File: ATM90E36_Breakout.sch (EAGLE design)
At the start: 71 parts, among them IC1 ATM90E36, J1 GREEN-2P-3.5, J2 ST-PJ-312, J3 ST-PJ-312, J4 GREEN-2P-3.5, J5 ST-PJ-312, J6 ST-PJ-312, Q1 FA-128

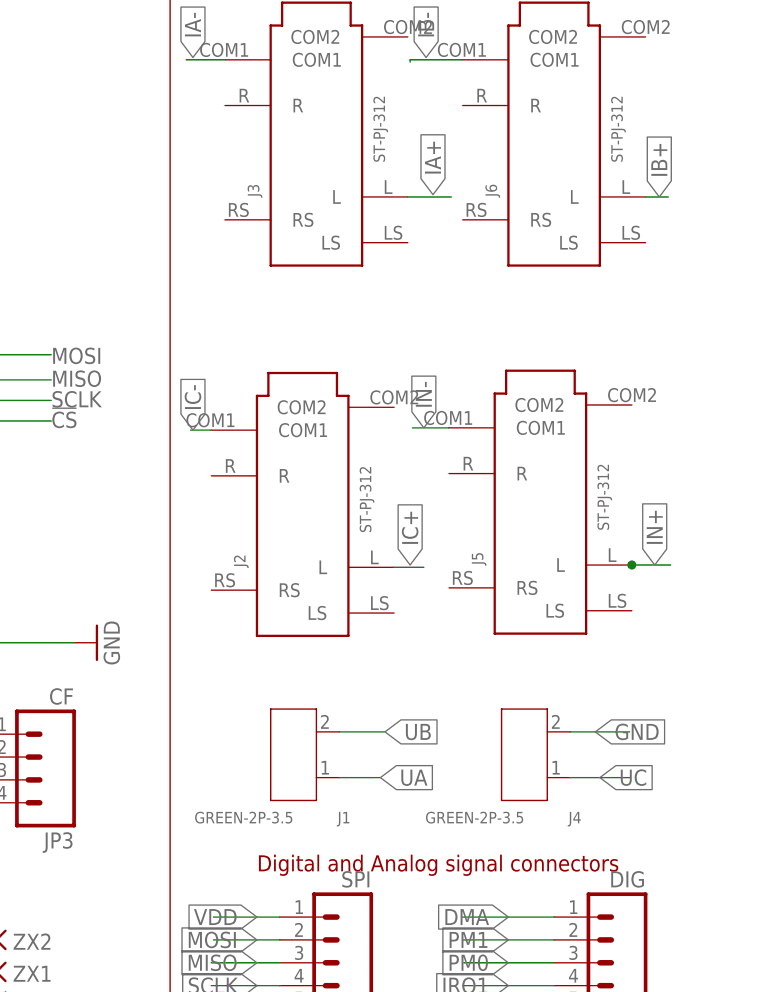
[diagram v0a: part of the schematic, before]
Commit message: Renamed CT's and improved cutouts
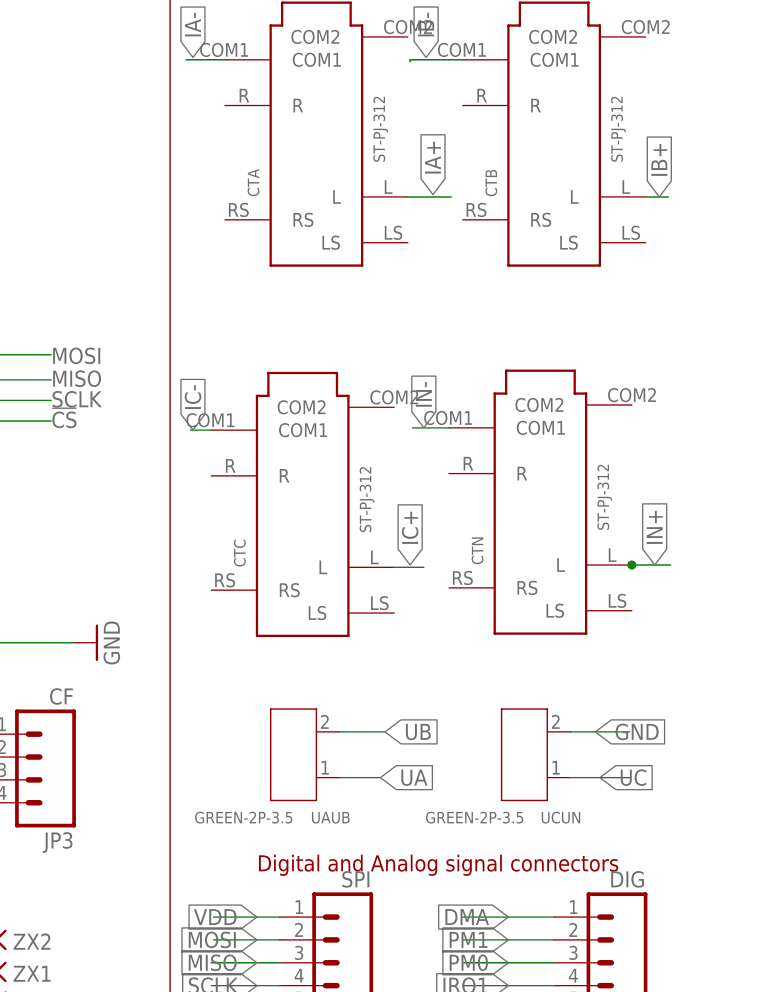
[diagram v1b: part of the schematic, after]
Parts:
- renumbered J1 to UAUB, J2 to CTC, J3 to CTA, J4 to UCUN, J5 to CTN, J6 to CTB
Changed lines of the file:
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@@
 <part name="R12" library="adafruit" deviceset="R-US_" device="R0603" value="100K"/>
 <part name="R14" library="adafruit" deviceset="R-US_" device="R0603" value="100K"/>
-<part name="J1" library="Seeed-Connector -2016" deviceset="SCREW-TERMINAL-GREEN(2P-3.5)" device="" value="GREEN-2P-3.5"/>
-<part name="J4" library="Seeed-Connector -2016" deviceset="SCREW-TERMINAL-GREEN(2P-3.5)" device="" value="GREEN-2P-3.5"/>
-<part name="J3" library="Seeed-Connector -2016" deviceset="AUDIO-JACK-6P-SMD(ST-PJ-312)" device="" value="ST-PJ-312"/>
-<part name="J6" library="Seeed-Connector -2016" deviceset="AUDIO-JACK-6P-SMD(ST-PJ-312)" device="" value="ST-PJ-312"/>
-<part name="J2" library="Seeed-Connector -2016" deviceset="AUDIO-JACK-6P-SMD(ST-PJ-312)" device="" value="ST-PJ-312"/>
-<part name="J5" library="Seeed-Connector -2016" deviceset="AUDIO-JACK-6P-SMD(ST-PJ-312)" device="" value="ST-PJ-312"/>
+<part name="UAUB" library="Seeed-Connector -2016" deviceset="SCREW-TERMINAL-GREEN(2P-3.5)" device="" value="GREEN-2P-3.5"/>
+<part name="UCUN" library="Seeed-Connector -2016" deviceset="SCREW-TERMINAL-GREEN(2P-3.5)" device="" value="GREEN-2P-3.5"/>
+<part name="CTA" library="Seeed-Connector -2016" deviceset="AUDIO-JACK-6P-SMD(ST-PJ-312)" device="" value="ST-PJ-312"/>
+<part name="CTB" library="Seeed-Connector -2016" deviceset="AUDIO-JACK-6P-SMD(ST-PJ-312)" device="" value="ST-PJ-312"/>
+<part name="CTC" library="Seeed-Connector -2016" deviceset="AUDIO-JACK-6P-SMD(ST-PJ-312)" device="" value="ST-PJ-312"/>
+<part name="CTN" library="Seeed-Connector -2016" deviceset="AUDIO-JACK-6P-SMD(ST-PJ-312)" device="" value="ST-PJ-312"/>
 <part name="JP2" library="SparkFun-Connectors" deviceset="M06" device="LOCK" value="DIG"/>
 <part name="JP1" library="SparkFun-Connectors" deviceset="M06" device="LOCK" value="SPI"/>
@@
 <instance part="R12" gate="G$1" x="43.18" y="141.986" rot="R90"/>
 <instance part="R14" gate="G$1" x="55.88" y="141.732" rot="R90"/>
-<instance part="J1" gate="G$1" x="230.124" y="91.694" rot="R180"/>
-<instance part="J4" gate="G$1" x="255.778" y="91.694" rot="R180"/>
-<instance part="J3" gate="G$1" x="232.664" y="160.02" smashed="yes" rot="R90">
+<instance part="UAUB" gate="G$1" x="230.124" y="91.694" rot="R180"/>
+<instance part="UCUN" gate="G$1" x="255.778" y="91.694" rot="R180"/>
+<instance part="CTA" gate="G$1" x="232.664" y="160.02" smashed="yes" rot="R90">
 <attribute name="NAME" x="226.314" y="153.67" size="1.27" layer="95" ratio="10" rot="R90"/>
 <attribute name="VALUE" x="240.284" y="157.48" size="1.27" layer="96" ratio="10" rot="R90"/>
 </instance>
-<instance part="J6" gate="G$1" x="259.08" y="160.02" smashed="yes" rot="R90">
+<instance part="CTB" gate="G$1" x="259.08" y="160.02" smashed="yes" rot="R90">
 <attribute name="NAME" x="252.73" y="153.67" size="1.27" layer="95" ratio="10" rot="R90"/>
 <attribute name="VALUE" x="266.7" y="157.48" size="1.27" layer="96" ratio="10" rot="R90"/>
 </instance>
-<instance part="J2" gate="G$1" x="231.14" y="118.872" smashed="yes" rot="R90">
+<instance part="CTC" gate="G$1" x="231.14" y="118.872" smashed="yes" rot="R90">
 <attribute name="NAME" x="224.79" y="112.522" size="1.27" layer="95" ratio="10" rot="R90"/>
 <attribute name="VALUE" x="238.76" y="116.332" size="1.27" layer="96" ratio="10" rot="R90"/>
 </instance>
-<instance part="J5" gate="G$1" x="257.556" y="119.126" smashed="yes" rot="R90">
+<instance part="CTN" gate="G$1" x="257.556" y="119.126" smashed="yes" rot="R90">
 <attribute name="NAME" x="251.206" y="112.776" size="1.27" layer="95" ratio="10" rot="R90"/>
 <attribute name="VALUE" x="265.176" y="116.586" size="1.27" layer="96" ratio="10" rot="R90"/>
@@
 </segment>
 <segment>
-<pinref part="J6" gate="G$1" pin="COM1"/>
+<pinref part="CTB" gate="G$1" pin="COM1"/>
 <wire x1="248.92" y1="168.91" x2="243.078" y2="168.91" width="0.1524" layer="91"/>
 <wire x1="243.078" y1="168.91" x2="243.078" y2="168.656" width="0.1524" layer="91"/>
@@
 </segment>
 <segment>
-<pinref part="J3" gate="G$1" pin="L"/>
+<pinref part="CTA" gate="G$1" pin="L"/>
 <wire x1="242.824" y1="153.67" x2="247.65" y2="153.67" width="0.1524" layer="91"/>
 <label x="245.618" y="153.924" size="1.778" layer="95" rot="R90" xref="yes"/>
@@
 </segment>
 <segment>
-<pinref part="J6" gate="G$1" pin="L"/>
+<pinref part="CTB" gate="G$1" pin="L"/>
 <wire x1="269.24" y1="153.67" x2="271.78" y2="153.67" width="0.1524" layer="91"/>
 <label x="270.764" y="153.67" size="1.778" layer="95" rot="R90" xref="yes"/>
@@
 </segment>
 <segment>
-<pinref part="J2" gate="G$1" pin="L"/>
+<pinref part="CTC" gate="G$1" pin="L"/>
 <wire x1="241.3" y1="112.522" x2="244.602" y2="112.522" width="0.1524" layer="91"/>
 <label x="243.078" y="112.776" size="1.778" layer="95" rot="R90" xref="yes"/>
@@
 </segment>
 <segment>
-<pinref part="J2" gate="G$1" pin="COM1"/>
+<pinref part="CTC" gate="G$1" pin="COM1"/>
 <wire x1="220.98" y1="127.762" x2="218.694" y2="127.762" width="0.1524" layer="91"/>
 <label x="218.948" y="127.762" size="1.778" layer="95" rot="R90" xref="yes"/>
@@
 </segment>
 <segment>
-<pinref part="J4" gate="G$1" pin="2"/>
+<pinref part="UCUN" gate="G$1" pin="2"/>
 <wire x1="260.858" y1="94.234" x2="267.462" y2="94.234" width="0.1524" layer="91"/>
 <label x="263.652" y="94.234" size="1.778" layer="95" xref="yes"/>
@@
 <wire x1="267.462" y1="112.776" x2="267.716" y2="112.776" width="0.1524" layer="91"/>
 <label x="270.256" y="112.776" size="1.778" layer="95" rot="R90" xref="yes"/>
-<pinref part="J5" gate="G$1" pin="L"/>
+<pinref part="CTN" gate="G$1" pin="L"/>
 <wire x1="267.716" y1="112.776" x2="272.034" y2="112.776" width="0.1524" layer="91"/>
 <junction x="267.716" y="112.776"/>
@@
 </segment>
 <segment>
-<pinref part="J5" gate="G$1" pin="COM1"/>
+<pinref part="CTN" gate="G$1" pin="COM1"/>
 <wire x1="247.396" y1="128.016" x2="243.332" y2="128.016" width="0.1524" layer="91"/>
 <label x="244.602" y="128.016" size="1.778" layer="95" rot="R90" xref="yes"/>
@@
 </segment>
 <segment>
-<pinref part="J3" gate="G$1" pin="COM1"/>
+<pinref part="CTA" gate="G$1" pin="COM1"/>
 <wire x1="222.504" y1="168.91" x2="218.186" y2="168.91" width="0.1524" layer="91"/>
 <label x="218.948" y="169.164" size="1.778" layer="95" rot="R90" xref="yes"/>
@@
 </segment>
 <segment>
-<pinref part="J1" gate="G$1" pin="1"/>
+<pinref part="UAUB" gate="G$1" pin="1"/>
 <wire x1="235.204" y1="89.154" x2="239.776" y2="89.154" width="0.1524" layer="91"/>
 <label x="239.776" y="89.154" size="1.778" layer="95" xref="yes"/>
@@
 <segment>
 <label x="240.284" y="94.234" size="1.778" layer="95" xref="yes"/>
-<pinref part="J1" gate="G$1" pin="2"/>
+<pinref part="UAUB" gate="G$1" pin="2"/>
 <wire x1="235.204" y1="94.234" x2="240.284" y2="94.234" width="0.1524" layer="91"/>
 </segment>
@@
 </segment>
 <segment>
-<pinref part="J4" gate="G$1" pin="1"/>
+<pinref part="UCUN" gate="G$1" pin="1"/>
 <wire x1="260.858" y1="89.154" x2="267.462" y2="89.154" width="0.1524" layer="91"/>
 <label x="264.16" y="89.154" size="1.778" layer="95" xref="yes"/>
